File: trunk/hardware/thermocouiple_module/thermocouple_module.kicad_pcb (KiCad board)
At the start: 2 copper layers, 19 x 27.9 mm, 9 parts, among them P1 CONN_2, P2 CONN_1, P3 CONN_4, P4 CONN_2, U5 MAX31855KASA

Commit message: 0.2
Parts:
- added P5: CONN_1, SCREW_TERM_534-7693, F.Cu at (99.1, 78.1)
- added P6: CONN_1, SCREW_TERM_534-7693, F.Cu at (110.5, 78.1)
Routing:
- net /TCPL-: track 14.4 -> 35.7 mm
- net /TCPL+: track 14.1 -> 35.5 mm
- net GND: track 32.5 -> 35.4 mm
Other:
- board text removed: "http://code.google.com/p/daecu/ for rusEFI"
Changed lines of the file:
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@@
 (kicad_pcb (version 3) (host pcbnew "(2013-07-07 BZR 4022)-stable")
   (general
-    (links 17)
+    (links 25)
     (no_connects 0)
     (area 93.7768 56.5658 124.877288 94.6912)
     (thickness 1.6002)
-    (drawings 15)
-    (tracks 44)
+    (drawings 14)
+    (tracks 54)
     (zones 0)
-    (modules 9)
+    (modules 11)
     (nets 8)
   )
-  (page A4)
+  (page A)
+  (title_block
+    (title "Thermocouple breakout")
+    (rev R0.2)
+    (company "rusEFI by DAECU")
+  )
   (layers
     (15 Front signal)
@@
       (outputformat 1)
       (mirror false)
-      (drillshape 1)
+      (drillshape 0)
       (scaleselection 1)
-      (outputdirectory gerbers/gerbers_Spin2/))
+      (outputdirectory thermocouple_gerbers))
   )
   (net 0 "")
@@
     )
   )
-  (gr_text "http://code.google.com/p/daecu/\nfor rusEFI    R 0.2" (at 104.775 81.28) (layer F.SilkS)
-    (effects (font (size 0.762 0.508) (thickness 0.127)))
-  )
-  (gr_text "http://code.google.com/p/daecu/\nfor rusEFI" (at 101.727 68.326 90) (layer B.SilkS)
+  (module SCREW_TERM_534-7693 (layer Front)
+    (at 99.06 78.105 180)
+    (fp_text reference P5 (at 0 -0.3175 180) (layer F.SilkS) hide
+      (effects (font (size 0.127 0.127) (thickness 0.00254)))
+    )
+    (fp_text value CONN_1 (at 0.09906 -0.8001 180) (layer F.SilkS) hide
+      (effects (font (size 0.127 0.127) (thickness 0.00254)))
+    )
+    (pad 1 thru_hole circle (at 2.5019 -3.5052 180) (size 2.286 2.286) (drill 1.9304)
+      (layers *.Cu *.Mask)
+      (net 5 /TCPL-)
+    )
+    (pad 1 thru_hole circle (at 2.5019 3.5052 180) (size 2.286 2.286) (drill 1.9304)
+      (layers *.Cu *.Mask)
+      (net 5 /TCPL-)
+    )
+    (pad 1 thru_hole circle (at -2.5019 3.5052 180) (size 2.286 2.286) (drill 1.9304)
+      (layers *.Cu *.Mask)
+      (net 5 /TCPL-)
+    )
+    (pad 1 thru_hole circle (at -2.5019 -3.5052 180) (size 2.286 2.286) (drill 1.9304)
+      (layers *.Cu *.Mask)
+      (net 5 /TCPL-)
+    )
+    (model 3D/screw_term_534-7693.wrl
+      (at (xyz 0 0 0.22))
+      (scale (xyz 10 10 10))
+      (rotate (xyz 270 0 90))
+    )
+  )
+  (module SCREW_TERM_534-7693 (layer Front)
+    (at 110.49 78.105 180)
+    (fp_text reference P6 (at 0 -0.3175 180) (layer F.SilkS) hide
+      (effects (font (size 0.127 0.127) (thickness 0.00254)))
+    )
+    (fp_text value CONN_1 (at 0.09906 -0.8001 180) (layer F.SilkS) hide
+      (effects (font (size 0.127 0.127) (thickness 0.00254)))
+    )
+    (pad 1 thru_hole circle (at 2.5019 -3.5052 180) (size 2.286 2.286) (drill 1.9304)
+      (layers *.Cu *.Mask)
+      (net 4 /TCPL+)
+    )
+    (pad 1 thru_hole circle (at 2.5019 3.5052 180) (size 2.286 2.286) (drill 1.9304)
+      (layers *.Cu *.Mask)
+      (net 4 /TCPL+)
+    )
+    (pad 1 thru_hole circle (at -2.5019 3.5052 180) (size 2.286 2.286) (drill 1.9304)
+      (layers *.Cu *.Mask)
+      (net 4 /TCPL+)
+    )
+    (pad 1 thru_hole circle (at -2.5019 -3.5052 180) (size 2.286 2.286) (drill 1.9304)
+      (layers *.Cu *.Mask)
+      (net 4 /TCPL+)
+    )
+    (model 3D/screw_term_534-7693.wrl
+      (at (xyz 0 0 0.22))
+      (scale (xyz 10 10 10))
+      (rotate (xyz 270 0 90))
+    )
+  )
+  (gr_text "http://code.google.com/p/daecu/\nfor rusEFI    R 0.2" (at 104.775 83.566) (layer B.SilkS)
     (effects (font (size 0.762 0.508) (thickness 0.127)) (justify mirror))
   )
@@
   (segment (start 108.585 60.325) (end 108.585 61.22924) (width 0.3048) (layer Front) (net 3))
   (segment (start 108.585 61.22924) (end 106.78414 63.0301) (width 0.3048) (layer Front) (net 3))
+  (segment (start 112.9919 74.5998) (end 107.9881 74.5998) (width 0.3048) (layer Front) (net 4))
+  (segment (start 112.9919 81.6102) (end 112.9919 74.5998) (width 0.3048) (layer Front) (net 4))
+  (segment (start 107.9881 81.6102) (end 107.9881 74.5998) (width 0.3048) (layer Front) (net 4))
+  (segment (start 106.045 73.66) (end 107.0483 73.66) (width 0.3048) (layer Front) (net 4))
+  (segment (start 107.0483 73.66) (end 107.9881 74.5998) (width 0.3048) (layer Front) (net 4))
   (segment (start 105.51414 68.3641) (end 105.51414 73.12914) (width 0.2032) (layer Front) (net 4))
   (segment (start 105.51414 73.12914) (end 106.045 73.66) (width 0.2032) (layer Front) (net 4))
@@
   (segment (start 105.64114 70.49516) (end 110.45952 70.49516) (width 0.508) (layer Front) (net 4))
   (segment (start 110.45952 70.49516) (end 111.57458 71.61022) (width 0.508) (layer Front) (net 4))
+  (segment (start 96.5581 74.5998) (end 101.5619 74.5998) (width 0.3048) (layer Front) (net 5))
+  (segment (start 101.5619 81.6102) (end 101.5619 74.5998) (width 0.3048) (layer Front) (net 5))
+  (segment (start 96.5581 81.6102) (end 96.5581 74.5998) (width 0.3048) (layer Front) (net 5))
+  (segment (start 103.505 73.66) (end 102.5017 73.66) (width 0.3048) (layer Front) (net 5))
+  (segment (start 102.5017 73.66) (end 101.5619 74.5998) (width 0.3048) (layer Front) (net 5))
   (segment (start 99.09048 70.49516) (end 97.97542 71.61022) (width 0.508) (layer Front) (net 5))
   (segment (start 104.11714 70.49516) (end 99.09048 70.49516) (width 0.508) (layer Front) (net 5))
@@
   (segment (start 106.78414 68.3641) (end 106.78414 66.31686) (width 0.3048) (layer Front) (net 6))
   (segment (start 106.78414 66.31686) (end 107.061 66.04) (width 0.3048) (layer Front) (net 6))
+  (segment (start 104.2035 66.04) (end 104.2035 68.5165) (width 0.3048) (layer Back) (net 7))
+  (via (at 104.775 78.74) (size 0.508) (layers Front Back) (net 7))
+  (segment (start 101.6 78.74) (end 104.775 78.74) (width 0.3048) (layer Back) (net 7))
+  (segment (start 99.06 76.2) (end 101.6 78.74) (width 0.3048) (layer Back) (net 7))
+  (segment (start 99.06 73.66) (end 99.06 76.2) (width 0.3048) (layer Back) (net 7))
+  (segment (start 104.2035 68.5165) (end 99.06 73.66) (width 0.3048) (layer Back) (net 7))
   (segment (start 107.3658 64.9224) (end 107.3404 64.9224) (width 0.3048) (layer Back) (net 7))
   (segment (start 107.3658 64.9224) (end 108.1786 65.7352) (width 0.3048) (layer Back) (net 7))
@@
   (segment (start 107.188 64.77) (end 104.648 64.77) (width 0.3048) (layer Back) (net 7))
   (segment (start 107.3404 64.9224) (end 107.188 64.77) (width 0.3048) (layer Back) (net 7))
-  (segment (start 104.2035 66.04) (end 104.2035 69.1515) (width 0.3048) (layer Back) (net 7))
-  (via (at 104.775 78.105) (size 0.508) (layers Front Back) (net 7))
-  (segment (start 102.87 78.105) (end 104.775 78.105) (width 0.3048) (layer Back) (net 7))
-  (segment (start 100.965 76.2) (end 102.87 78.105) (width 0.3048) (layer Back) (net 7))
-  (segment (start 100.965 72.39) (end 100.965 76.2) (width 0.3048) (layer Back) (net 7))
-  (segment (start 104.2035 69.1515) (end 100.965 72.39) (width 0.3048) (layer Back) (net 7))
   (segment (start 102.97414 68.3641) (end 102.97414 65.12814) (width 0.3048) (layer Front) (net 7))
   (segment (start 98.806 60.96) (end 97.79 60.96) (width 0.3048) (layer Front) (net 7))

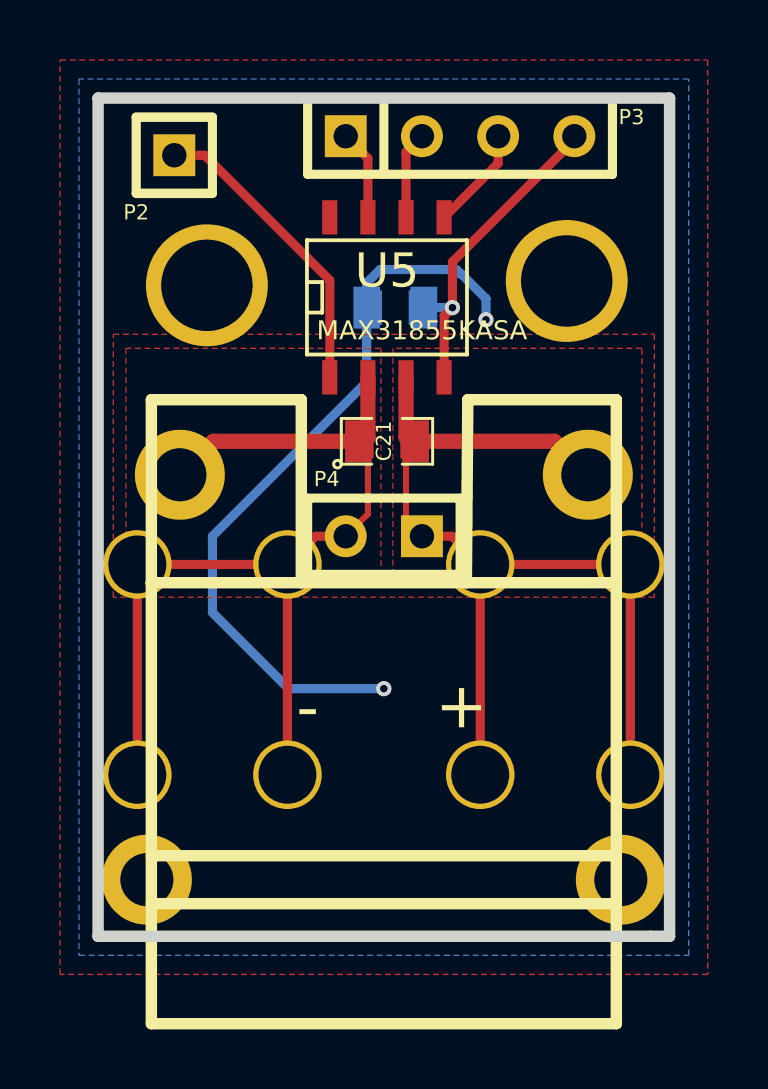
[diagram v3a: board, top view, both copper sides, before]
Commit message: 
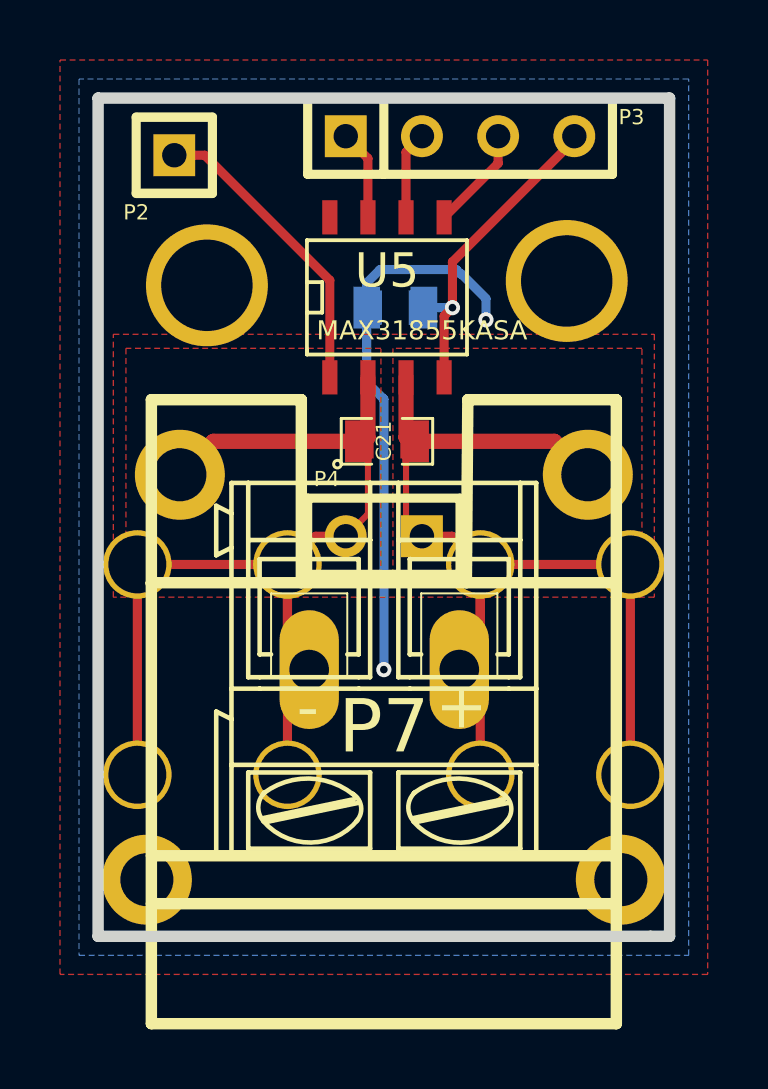
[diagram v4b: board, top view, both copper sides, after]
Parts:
- added P7: CONN_2, AK300-2, F.Cu at (104.8, 78.1)
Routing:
- net GND: track 35.4 -> 28.7 mm
- net /TCPL-: track 35.7 -> 39.6 mm
- net /TCPL+: track 35.5 -> 39.2 mm
